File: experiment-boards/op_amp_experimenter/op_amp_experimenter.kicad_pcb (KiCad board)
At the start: 2 copper layers, 85.1 x 72.8 mm, 49 parts, among them J1 Conn_01x03_Pin, J10 Conn_01x03_Pin, J11 Conn_01x03_Pin, J12 Conn_01x03_Pin, J14 Conn_02x05_Odd_Even, J15 Conn_02x05_Odd_Even, J2 Conn_01x04_Pin, J3 Conn_01x04_Pin, J4 Conn_01x04_Pin, J5 Conn_01x04_Pin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

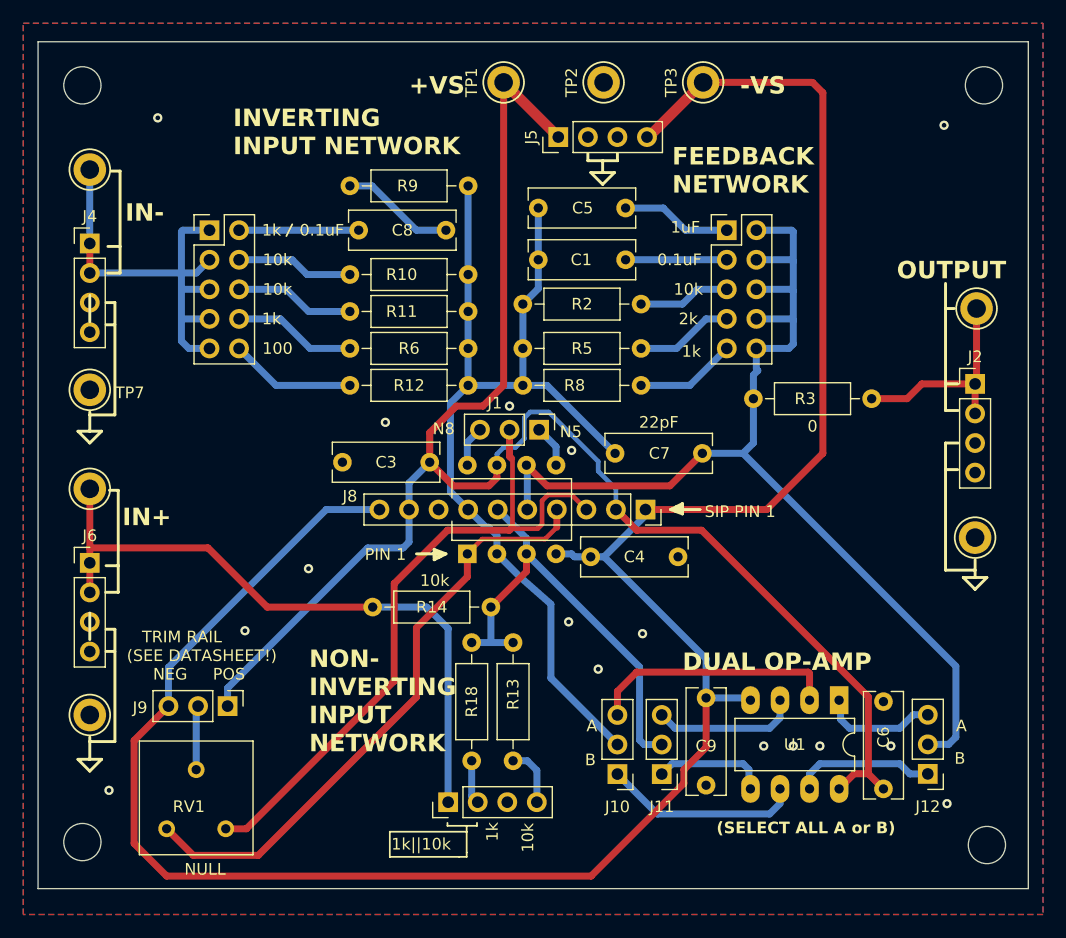
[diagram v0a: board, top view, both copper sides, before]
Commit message: Put accessory boards in directories. Add LTspice. Add gerbers. Add 45W power supply.
Signed-off-by: Mark Thoren <mark.thoren@analog.com>
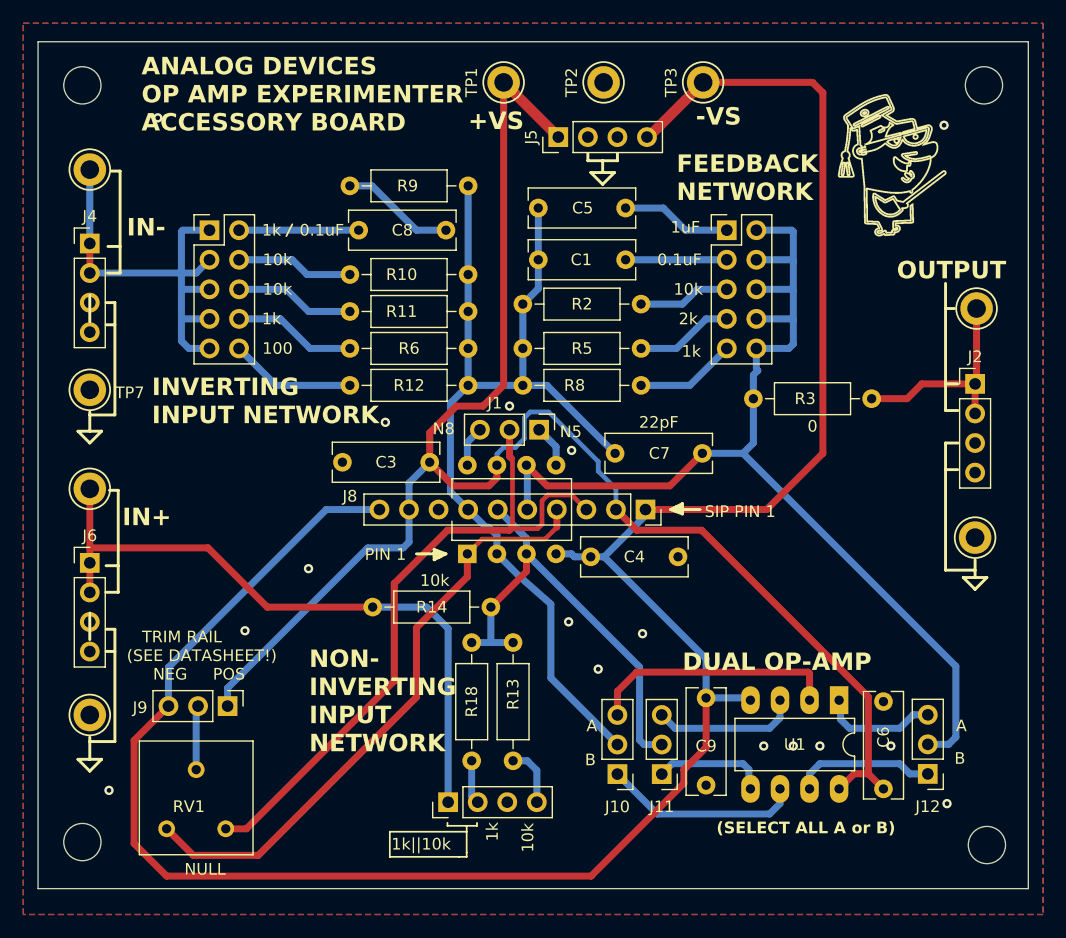
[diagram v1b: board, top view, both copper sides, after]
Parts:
- added U$1: PROFF, lumped-transmission-line:PROFF, F.Cu at (174.5, 72.3)
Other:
- board text added: "ANALOG DEVICES OP AMP EXPERIMENTER ACCESSORY BOARD"
- board text added: "https://github.com/analogdevicesinc/education_tools/"
- board text added: "wiki.analog.com/university"
